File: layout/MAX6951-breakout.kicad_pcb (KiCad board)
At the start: 2 copper layers, 18.8 x 23.9 mm, 7 parts, among them J1 Conn_01x09_Male, J2 Conn_01x05_Male, U1 MAX6951

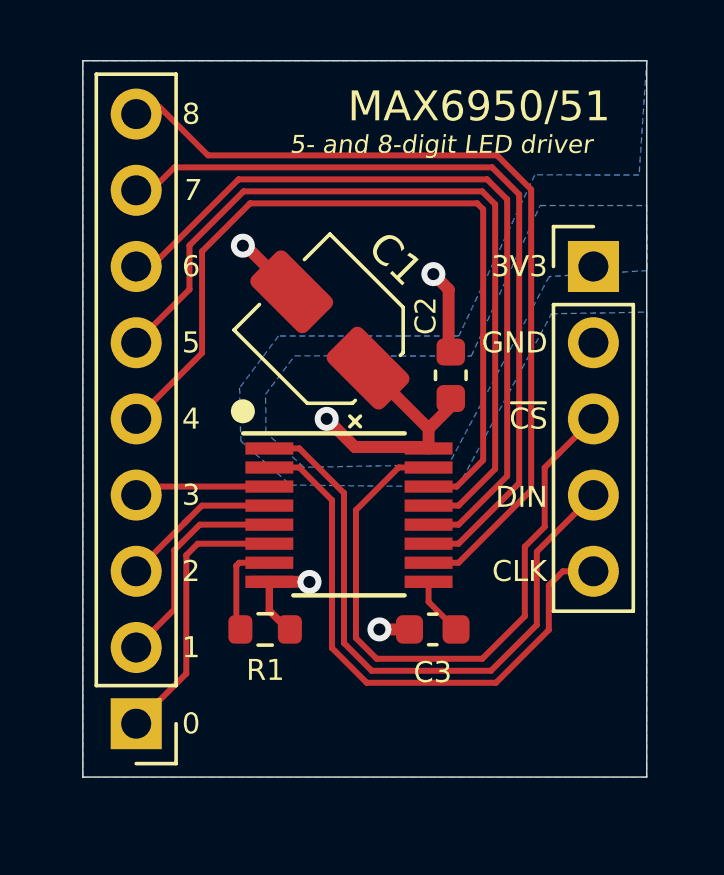
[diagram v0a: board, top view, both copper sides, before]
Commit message: Update schematic and PCB to include thermal pad
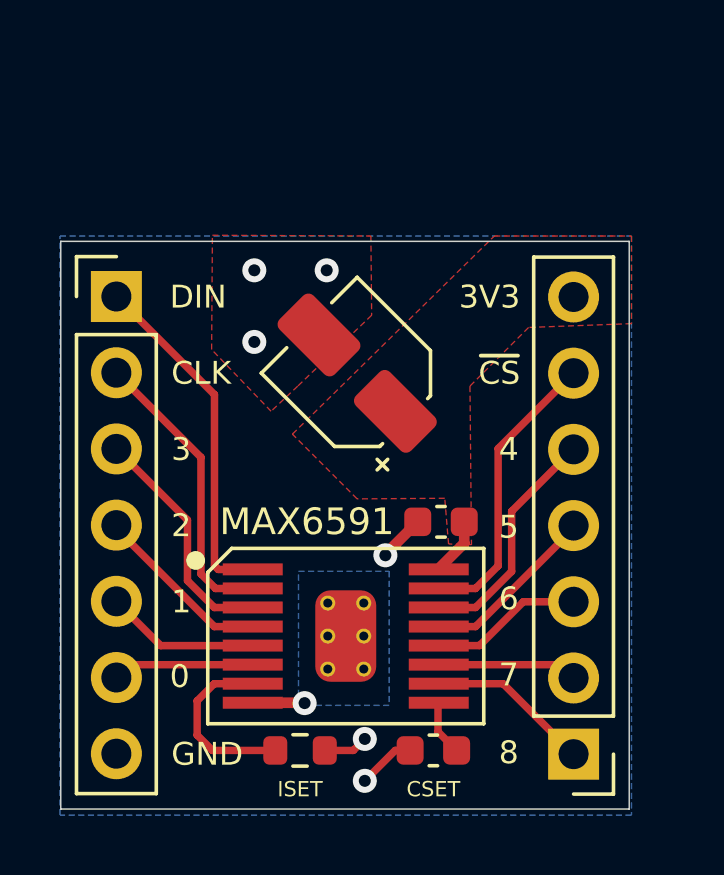
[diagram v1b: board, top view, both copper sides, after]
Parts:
- removed U1: MAX6951, Package_SO:QSOP-16_3.9x4.9mm_P0.635mm
- added G***: LOGO, LOGO, B.Cu at (142.6, 101.0)
- added MAX6591: MAX6951_ThermalVias, Package_SO:MAX6951_ThermalVias, F.Cu at (145.7, 105.3)
- J1: value Conn_01x09_Male -> Conn_01x07_Female; footprint Connector_PinHeader_2.54mm:PinHeader_1x09_P2.54mm_Vertical -> Connector_PinHeader_2.54mm:PinHeader_1x07_P2.54mm_Vertical
- J2: value Conn_01x05_Male -> Conn_01x07_Female; footprint Connector_PinHeader_2.54mm:PinHeader_1x05_P2.54mm_Vertical -> Connector_PinHeader_2.54mm:PinHeader_1x07_P2.54mm_Vertical
- moved J2 16.3 mm to (153.3, 109.2), turned to 180 degrees
- moved J1 14.3 mm to (138.0, 94.0), turned to 0 degrees
- moved C2 4.90 mm to (148.8, 101.5), turned to 180 degrees
- moved R1 4.20 mm to (144.1, 109.1)
- moved C3 4.03 mm to (148.6, 109.1)
- moved C1 1.70 mm to (146.1, 96.5)
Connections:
- J1 pad 1: SEG0 -> DIN
- J1 pad 2: SEG1 -> CLK
- J1 pad 3: SEG2 -> SEG3
- J1 pad 4: SEG3 -> SEG2
- J1 pad 5: SEG4 -> SEG1
- J1 pad 6: SEG5 -> SEG0
- J1 pad 7: SEG6 -> GND
- J2 pad 1: +3V3 -> SEG8
- J2 pad 2: GND -> SEG7
- J2 pad 3: ~CS -> SEG6
- J2 pad 4: DIN -> SEG5
- J2 pad 5: CLK -> SEG4
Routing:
- net SEG8: track 28.0 -> 5.49 mm
- net SEG7: track 26.1 -> 4.70 mm
- net ~CS: track 21.3 -> 0.00 mm
- net SEG5: track 26.6 -> 5.97 mm
- net SEG6: track 25.5 -> 5.10 mm
- net SEG4: track 27.4 -> 7.88 mm
- net ~{CS}: track 0.00 -> 9.78 mm
- net CLK: track 19.4 -> 9.78 mm
- net DIN: track 20.7 -> 11.6 mm
- net +3V3: track 9.36 -> 1.95 mm, vias 1 -> 0
- net SEG0: track 9.24 -> 4.70 mm
- net GND: track 10.3 -> 7.08 mm, vias 4 -> 7
- net SEG3: track 5.26 -> 7.89 mm
- net ISET: track 3.41 -> 6.02 mm
- net SEG1: track 7.29 -> 5.13 mm
- added copper zone on F.Cu, net +3V3
- added copper zone on F.Cu, net GND
- removed copper zone on B.Cu, net +3V3
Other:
- board size 18.8 x 23.9 mm -> 18.9 x 18.9 mm
- net class Default removed
- board text added: "CSET"
- board text added: "ISET"
- board text added: "MAX6951 Breakout, v1 by Jed Parsons github.com/jedp/"
- board text added: "~{CS}"
- board text removed: "() 6951 only"
- board text removed: "(DIG5)/SEG5"
- board text removed: "(DIG6)/SEG6"
- board text removed: "(DIG7)/SEG7"
- board text removed: "5- and 8-digit LED driver"
- board text removed: "DIG0/SEG0"
- board text removed: "DIG1/SEG1"
- board text removed: "DIG2/SEG2"
- board text removed: "DIG3/SEG3"
- board text removed: "DIG4/SEG4"
- board text removed: "Jed Parsons"
- board text removed: "MAX6950/51"
- board text removed: "SEG8"
- board text removed: "~CS"

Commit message: Correct board layout of ISET
    See Board Layout on datasheet page 16 and Figure 5.
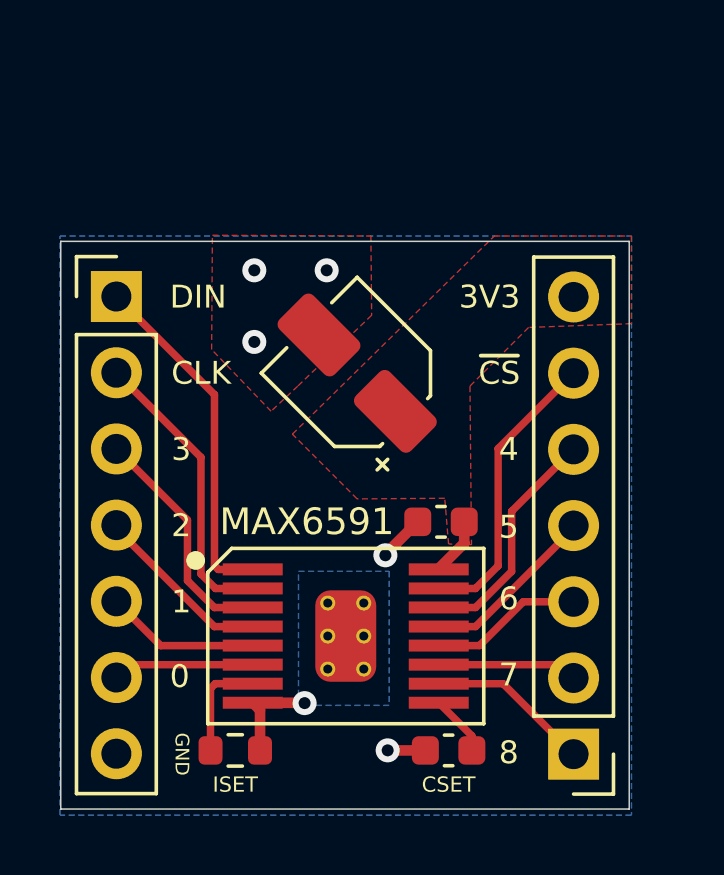
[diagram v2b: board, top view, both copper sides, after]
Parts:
- moved R1 2.16 mm to (142.0, 109.1)
- moved C3 0.51 mm to (149.1, 109.1)
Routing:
- net ISET: track 6.02 -> 3.54 mm
- net GND: track 7.08 -> 6.61 mm, vias 7 -> 6
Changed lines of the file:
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@@
   (net 16 "ISET")
   (footprint "Resistor_SMD:R_0603_1608Metric" (layer "F.Cu")
-    (at 144.145 109.095)
+    (at 141.986 109.095)
     (descr "Resistor SMD 0603 (1608 Metric), square (rectangular) end terminal, IPC_7351 nominal, (Body size source: IPC-SM-782 page 72, https://www.pcb-3d.com/wordpress/wp-content/uploads/ipc-sm-782a_amendment_1_and_2.pdf), generated with kicad-footprint-generator")
     (tags "resistor")
@@
   )
   (footprint "Capacitor_SMD:C_0603_1608Metric" (layer "F.Cu")
-    (at 148.59 109.095 180)
+    (at 149.098 109.095 180)
     (descr "Capacitor SMD 0603 (1608 Metric), square (rectangular) end terminal, IPC_7351 nominal, (Body size source: IPC-SM-782 page 76, https://www.pcb-3d.com/wordpress/wp-content/uploads/ipc-sm-782a_amendment_1_and_2.pdf), generated with kicad-footprint-generator")
     (tags "capacitor")
@@
     (effects (font (size 0.762 0.762) (thickness 0.127)) (justify right))
   )
-  (gr_text "ISET" (at 144.145 110.3884) (layer "F.SilkS")
+  (gr_text "ISET" (at 141.986 110.236) (layer "F.SilkS")
     (effects (font (size 0.508 0.508) (thickness 0.0762)))
   )
@@
     (effects (font (size 0.762 0.762) (thickness 0.127)) (justify left))
   )
-  (gr_text "CSET" (at 148.59 110.3884) (layer "F.SilkS")
+  (gr_text "CSET" (at 149.098 110.236) (layer "F.SilkS")
     (effects (font (size 0.508 0.508) (thickness 0.0762)))
   )
@@
     (effects (font (size 0.762 0.762) (thickness 0.127)) (justify right))
   )
-  (gr_text "GND" (at 139.8524 109.22) (layer "F.SilkS")
-    (effects (font (size 0.762 0.762) (thickness 0.127)) (justify left))
+  (gr_text "GND" (at 140.208 109.22 270) (layer "F.SilkS")
+    (effects (font (size 0.4572 0.4572) (thickness 0.0762)))
   )
   (gr_text "0" (at 139.8016 106.6292) (layer "F.SilkS")
@@
   (segment (start 149.619 102.1871) (end 148.7436 103.0625) (width 0.3556) (layer "F.Cu") (net 1))
   (segment (start 149.619 101.475) (end 149.619 102.1871) (width 0.3556) (layer "F.Cu") (net 1))
+  (segment (start 142.811 107.7475) (end 142.569 107.5055) (width 0.3556) (layer "F.Cu") (net 2))
   (segment (start 146.9898 102.5542) (end 148.069 101.475) (width 0.3556) (layer "F.Cu") (net 2))
-  (segment (start 144.97 109.095) (end 145.921 109.095) (width 0.25) (layer "F.Cu") (net 2))
-  (segment (start 147.815 109.095) (end 147.318 109.095) (width 0.25) (layer "F.Cu") (net 2))
+  (segment (start 147.068 109.095) (end 147.066 109.093) (width 0.3556) (layer "F.Cu") (net 2))
+  (segment (start 148.323 109.095) (end 147.068 109.095) (width 0.3556) (layer "F.Cu") (net 2))
   (segment (start 144.2847 107.5055) (end 144.2974 107.5182) (width 0.3556) (layer "F.Cu") (net 2))
   (segment (start 142.569 107.5055) (end 144.2847 107.5055) (width 0.3556) (layer "F.Cu") (net 2))
+  (segment (start 142.811 109.095) (end 142.811 107.7475) (width 0.3556) (layer "F.Cu") (net 2))
   (segment (start 145.034 94.990416) (end 144.777208 95.247208) (width 0.3556) (layer "F.Cu") (net 2))
   (segment (start 146.9898 102.5906) (end 146.9898 102.5542) (width 0.3556) (layer "F.Cu") (net 2))
-  (segment (start 147.318 109.095) (end 146.304 110.109) (width 0.25) (layer "F.Cu") (net 2))
-  (segment (start 145.921 109.095) (end 146.304 108.712) (width 0.25) (layer "F.Cu") (net 2))
   (via (at 145.034 93.091) (size 0.8) (drill 0.4) (layers "F.Cu" "B.Cu") (free) (net 2))
   (via (at 142.621 93.091) (size 0.8) (drill 0.4) (layers "F.Cu" "B.Cu") (free) (net 2))
-  (via (at 146.304 108.712) (size 0.8) (drill 0.4) (layers "F.Cu" "B.Cu") (free) (net 2))
-  (via (at 146.304 110.109) (size 0.8) (drill 0.4) (layers "F.Cu" "B.Cu") (free) (net 2))
+  (via (at 147.066 109.093) (size 0.8) (drill 0.4) (layers "F.Cu" "B.Cu") (free) (net 2))
   (via (at 142.621 95.4786) (size 0.8) (drill 0.4) (layers "F.Cu" "B.Cu") (free) (net 2))
   (via (at 144.2974 107.5182) (size 0.8) (drill 0.4) (layers "F.Cu" "B.Cu") (free) (net 2))
@@
   (segment (start 141.4165 103.0625) (end 141.293 102.939) (width 0.25) (layer "F.Cu") (net 14))
   (segment (start 141.293 97.2344) (end 138.0236 93.965) (width 0.25) (layer "F.Cu") (net 14))
-  (segment (start 148.7436 108.4736) (end 149.365 109.095) (width 0.25) (layer "F.Cu") (net 15))
-  (segment (start 148.7436 108.4736) (end 148.7436 107.5075) (width 0.25) (layer "F.Cu") (net 15))
-  (segment (start 142.5436 106.8725) (end 141.2855 106.8725) (width 0.25) (layer "F.Cu") (net 16))
-  (segment (start 141.226 109.095) (end 143.32 109.095) (width 0.25) (layer "F.Cu") (net 16))
-  (segment (start 141.2855 106.8725) (end 140.716 107.442) (width 0.25) (layer "F.Cu") (net 16))
-  (segment (start 140.716 107.442) (end 140.716 108.585) (width 0.25) (layer "F.Cu") (net 16))
-  (segment (start 140.716 108.585) (end 141.226 109.095) (width 0.25) (layer "F.Cu") (net 16))
+  (segment (start 149.873 108.6095) (end 148.769 107.5055) (width 0.25) (layer "F.Cu") (net 15))
+  (segment (start 149.873 109.095) (end 149.873 108.6095) (width 0.25) (layer "F.Cu") (net 15))
+  (segment (start 141.161 109.095) (end 141.161 107.0285) (width 0.25) (layer "F.Cu") (net 16))
+  (segment (start 141.319 106.8705) (end 142.569 106.8705) (width 0.25) (layer "F.Cu") (net 16))
+  (segment (start 141.161 107.0285) (end 141.319 106.8705) (width 0.25) (layer "F.Cu") (net 16))
   (zone (net 2) (net_name "GND") (layer "F.Cu") (hatch edge 0.508)
     (connect_pads (clearance 0.508))

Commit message: Fix crucial typo
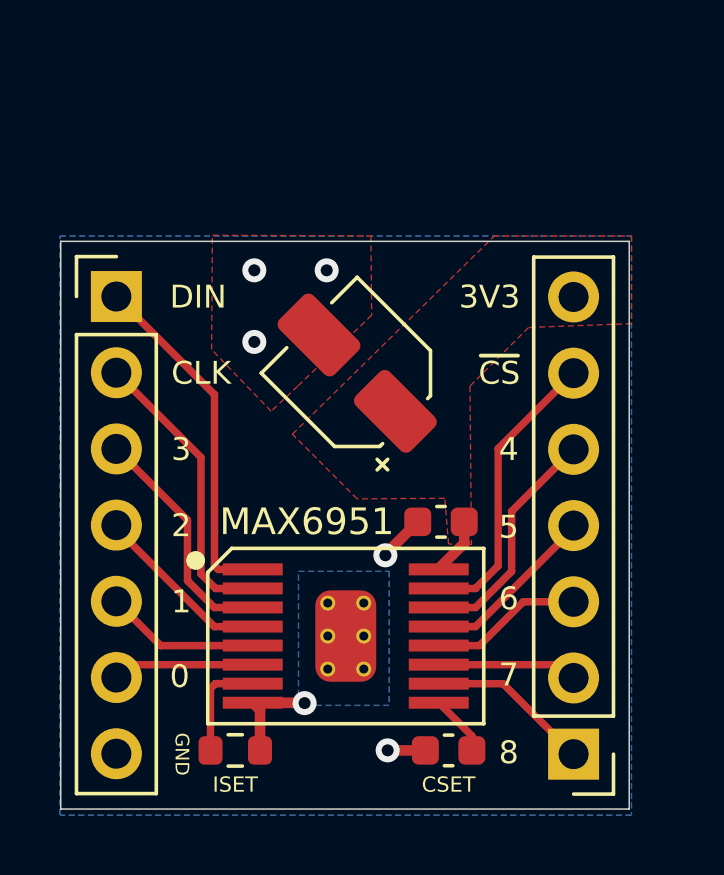
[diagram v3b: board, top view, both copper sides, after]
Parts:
- renumbered MAX6591 to MAX6951
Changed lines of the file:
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@@
     (property "Sheetname" "")
     (attr smd)
-    (fp_text reference "MAX6591" (at -3.81 1.2954) (layer "F.SilkS")
+    (fp_text reference "MAX6951" (at -3.81 1.2954) (layer "F.SilkS")
       (effects (font (size 0.889 0.889) (thickness 0.1397)))
     )
